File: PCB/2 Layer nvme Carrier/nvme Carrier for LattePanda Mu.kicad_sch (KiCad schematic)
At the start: 8 parts

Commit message: Parts change for BOM
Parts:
- H71, H72, H73, H74: footprint A_HDJ_Library:MountingHole_3.2mm_M3_Pad_Via -> MountingHole:MountingHole_4mm_Pad_Via
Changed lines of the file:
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@@
 			)
 		)
-		(property "Footprint" "A_HDJ_Library:MountingHole_3.2mm_M3_Pad_Via"
+		(property "Footprint" "MountingHole:MountingHole_4mm_Pad_Via"
 			(at 557.53 336.55 0)
 			(effects
@@
 		)
 		(property "Sim.Type" ""
+			(at 557.53 336.55 0)
+			(effects
+				(font
+					(size 1.27 1.27)
+				)
+				(hide yes)
+			)
+		)
+		(property "Mfr.# " ""
+			(at 557.53 336.55 0)
+			(effects
+				(font
+					(size 1.27 1.27)
+				)
+				(hide yes)
+			)
+		)
+		(property "Part#" ""
 			(at 557.53 336.55 0)
 			(effects
@@
 			)
 		)
+		(property "Mfr.# " ""
+			(at 473.71 336.55 0)
+			(effects
+				(font
+					(size 1.27 1.27)
+				)
+				(hide yes)
+			)
+		)
+		(property "Part#" ""
+			(at 473.71 336.55 0)
+			(effects
+				(font
+					(size 1.27 1.27)
+				)
+				(hide yes)
+			)
+		)
 		(pin "1"
 		)
@@
 			)
 		)
-		(property "Footprint" "A_HDJ_Library:MountingHole_3.2mm_M3_Pad_Via"
+		(property "Footprint" "MountingHole:MountingHole_4mm_Pad_Via"
 			(at 532.13 349.25 0)
 			(effects
@@
 		)
 		(property "Sim.Type" ""
+			(at 532.13 349.25 0)
+			(effects
+				(font
+					(size 1.27 1.27)
+				)
+				(hide yes)
+			)
+		)
+		(property "Mfr.# " ""
+			(at 532.13 349.25 0)
+			(effects
+				(font
+					(size 1.27 1.27)
+				)
+				(hide yes)
+			)
+		)
+		(property "Part#" ""
 			(at 532.13 349.25 0)
 			(effects
@@
 			)
 		)
+		(property "Mfr.# " ""
+			(at 499.11 349.25 0)
+			(effects
+				(font
+					(size 1.27 1.27)
+				)
+				(hide yes)
+			)
+		)
+		(property "Part#" ""
+			(at 499.11 349.25 0)
+			(effects
+				(font
+					(size 1.27 1.27)
+				)
+				(hide yes)
+			)
+		)
 		(pin "1"
 		)
@@
 			)
 		)
-		(property "Footprint" "A_HDJ_Library:MountingHole_3.2mm_M3_Pad_Via"
+		(property "Footprint" "MountingHole:MountingHole_4mm_Pad_Via"
 			(at 532.13 336.55 0)
 			(effects
@@
 		)
 		(property "Sim.Type" ""
+			(at 532.13 336.55 0)
+			(effects
+				(font
+					(size 1.27 1.27)
+				)
+				(hide yes)
+			)
+		)
+		(property "Mfr.# " ""
+			(at 532.13 336.55 0)
+			(effects
+				(font
+					(size 1.27 1.27)
+				)
+				(hide yes)
+			)
+		)
+		(property "Part#" ""
 			(at 532.13 336.55 0)
 			(effects
@@
 			)
 		)
-		(property "Footprint" "A_HDJ_Library:MountingHole_3.2mm_M3_Pad_Via"
+		(property "Footprint" "MountingHole:MountingHole_4mm_Pad_Via"
 			(at 557.53 349.25 0)
 			(effects
@@
 		)
 		(property "Sim.Type" ""
+			(at 557.53 349.25 0)
+			(effects
+				(font
+					(size 1.27 1.27)
+				)
+				(hide yes)
+			)
+		)
+		(property "Mfr.# " ""
+			(at 557.53 349.25 0)
+			(effects
+				(font
+					(size 1.27 1.27)
+				)
+				(hide yes)
+			)
+		)
+		(property "Part#" ""
 			(at 557.53 349.25 0)
 			(effects
@@
 			)
 		)
+		(property "Mfr.# " ""
+			(at 473.71 349.25 0)
+			(effects
+				(font
+					(size 1.27 1.27)
+				)
+				(hide yes)
+			)
+		)
+		(property "Part#" ""
+			(at 473.71 349.25 0)
+			(effects
+				(font
+					(size 1.27 1.27)
+				)
+				(hide yes)
+			)
+		)
 		(pin "1"
 		)
@@
 			(at 499.11 336.55 0)
 			(effects
+				(font
+					(size 1.27 1.27)
+				)
+				(hide yes)
+			)
+		)
+		(property "Mfr.# " ""
+			(at 499.11 336.55 0)
+			(effects
+				(font
+					(size 1.27 1.27)
+				)
+				(hide yes)
+			)
+		)
+		(property "Part#" ""
+			(at 499.11 336.55 0)
+			(effects

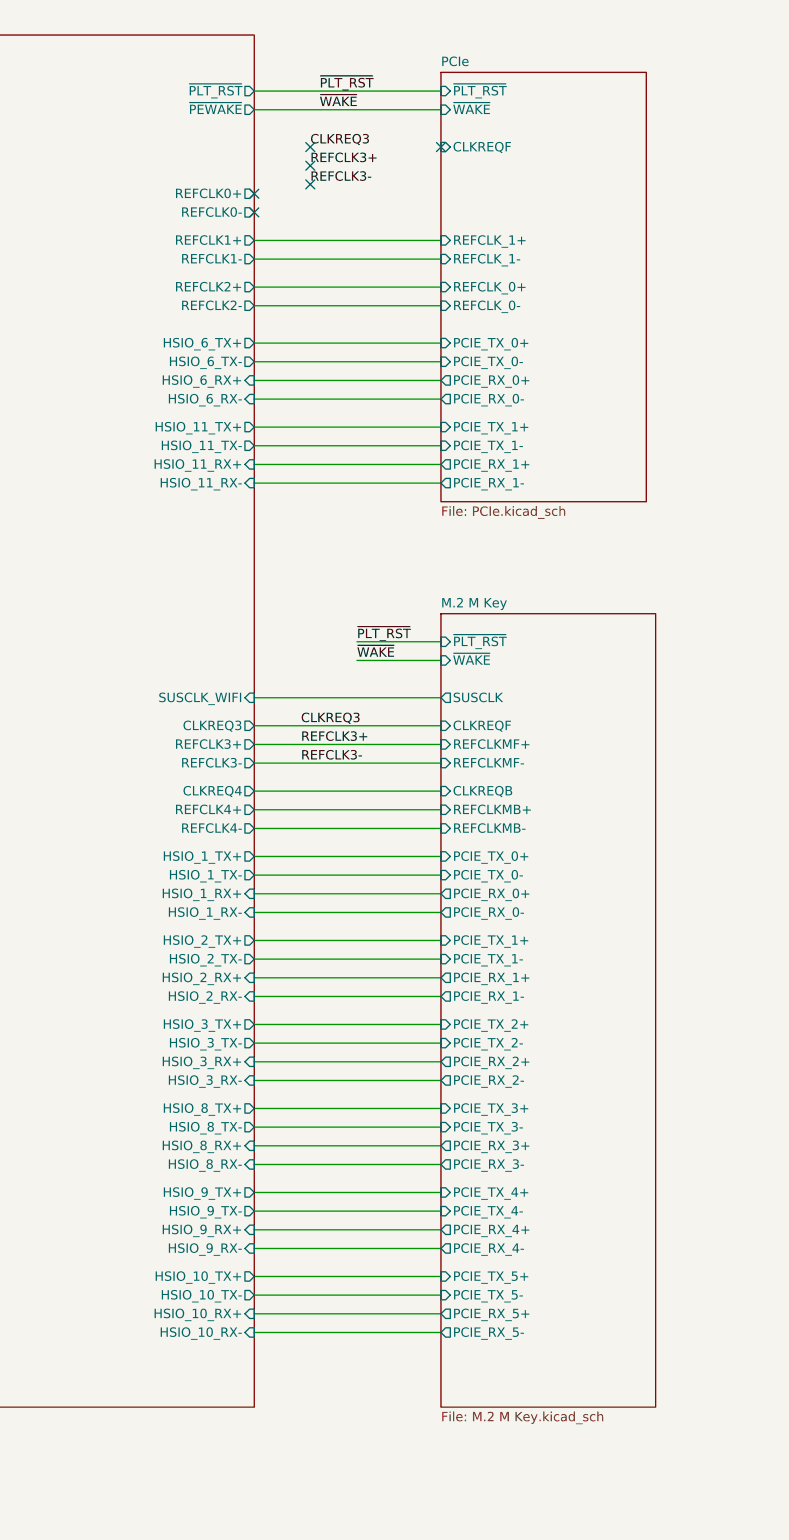
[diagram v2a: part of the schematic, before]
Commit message: Rework for PSU and REFCLK
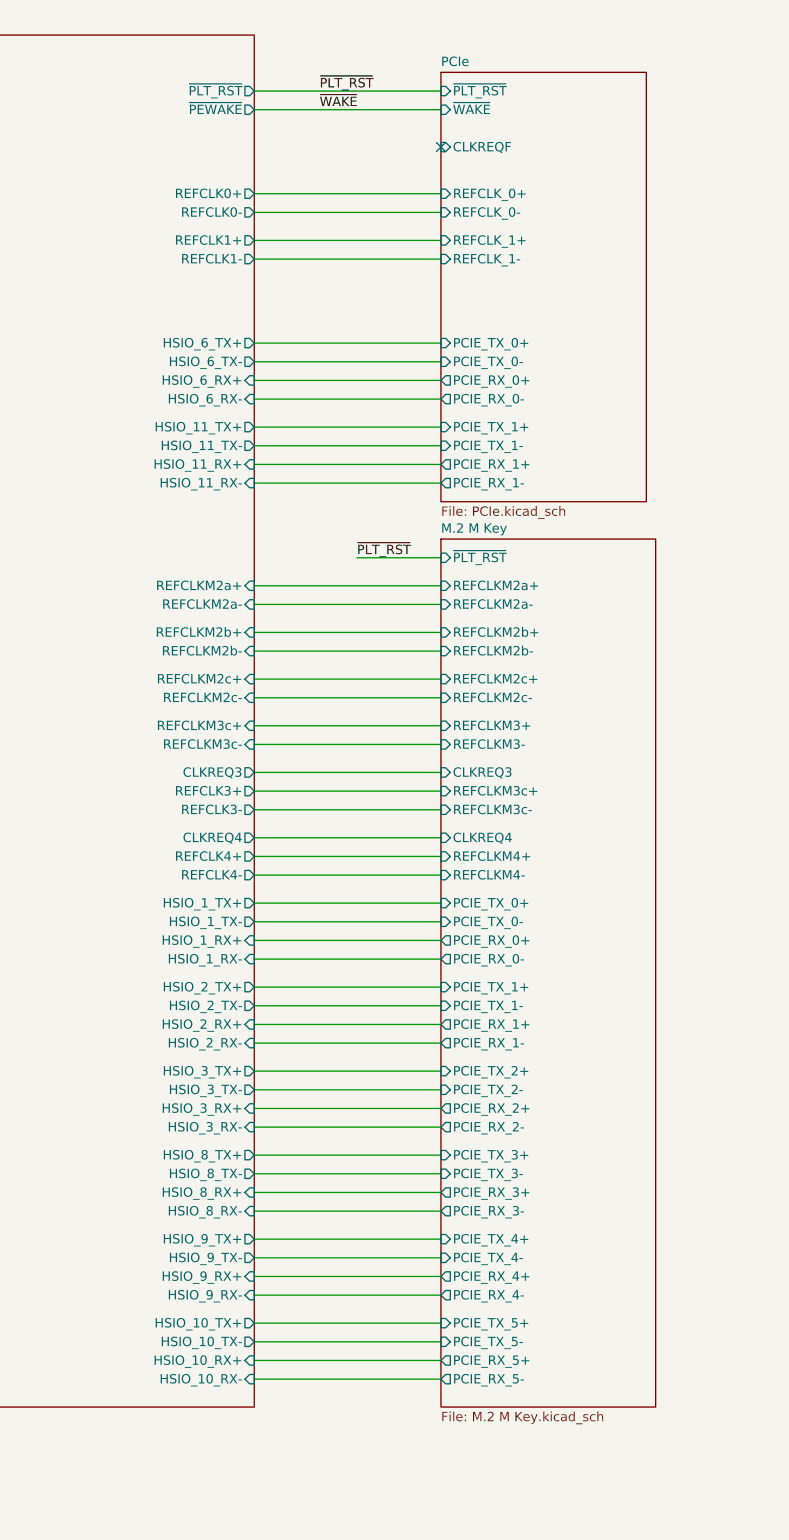
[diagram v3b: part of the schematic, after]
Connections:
- no-connect marks 7 -> 2
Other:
- sheet LattePanda Module ports: added REFCLKM2a+, REFCLKM2a-, REFCLKM2b+, REFCLKM2b-, REFCLKM2c+, REFCLKM2c-, REFCLKM3c+, REFCLKM3c-; removed REFCLK2+, REFCLK2-, SUSCLK_WIFI
- sheet M.2 M Key ports: added CLKREQ3, CLKREQ4, REFCLKM2a+, REFCLKM2a-, REFCLKM2b+, REFCLKM2b-, REFCLKM2c+, REFCLKM2c-, REFCLKM3+, REFCLKM3-, REFCLKM3c+, REFCLKM3c-, REFCLKM4+, REFCLKM4-; removed CLKREQB, CLKREQF, REFCLKMB+, REFCLKMB-, REFCLKMF+, REFCLKMF-, SUSCLK, ~{WAKE}

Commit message: Rework started with PCIe
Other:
- added sheet BIOS (BIOS.kicad_sch)
- added sheet PCIe CLK Buffer (PCIe CLK Buffer.kicad_sch)
- sheet LattePanda Module ports: added REFCLK2+, REFCLK2-, SPI-CS, SPI-IO0, SPI-IO1, SPI-IO2, SPI-IO3, SPI_CLK; removed REFCLKM2a+, REFCLKM2a-, REFCLKM2b+, REFCLKM2b-, REFCLKM2c+, REFCLKM2c-, REFCLKM3c+, REFCLKM3c-
- sheet M.2 M Key ports: added CLKREQM0, CLKREQM1, CLKREQM2, CLKREQM3, ~{WAKE}; removed none

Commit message: PCIe and CLK Buffenr Lines
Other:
- sheet M.2 M Key ports: added CLKREQM4, CLKREQM5, REFCLKM0+, REFCLKM0-, REFCLKM1+, REFCLKM1-, REFCLKM2+, REFCLKM2-, REFCLKM5+, REFCLKM5-; removed CLKREQ3, CLKREQ4, REFCLKM2a+, REFCLKM2a-, REFCLKM2b+, REFCLKM2b-, REFCLKM2c+, REFCLKM2c-, REFCLKM3c+, REFCLKM3c-
- sheet PCIe CLK Buffer ports: added CLKREQB0, CLKREQB1, CLKREQB2, CLKREQB3, REFCLKB0+, REFCLKB0-, REFCLKB1+, REFCLKB1-, REFCLKB2+, REFCLKB2-, REFCLKB3+, REFCLKB3-, REFCLK_IN+, REFCLK_IN-; removed CLKREQM0, CLKREQM1, CLKREQM2, CLKREQM3, REFCLK2+, REFCLK2-, REFCLKM0+, REFCLKM0-, REFCLKM1+, REFCLKM1-, REFCLKM2+, REFCLKM2-, REFCLKM3+, REFCLKM3-
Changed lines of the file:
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@@
 			)
 		)
-		(pin "CLKREQ3" output
+		(pin "CLKREQM0" output
 			(at 367.03 265.43 180)
 			(effects
@@
 			)
 		)
-		(pin "REFCLKM2c+" input
+		(pin "REFCLKM4+" input
 			(at 367.03 331.47 180)
 			(effects
@@
 			)
 		)
-		(pin "REFCLKM2c-" input
+		(pin "REFCLKM4-" input
 			(at 367.03 334.01 180)
 			(effects
@@
 			)
 		)
+		(pin "REFCLKM5+" input
+			(at 367.03 340.36 180)
+			(effects
+				(font
+					(size 1.27 1.27)
+				)
+				(justify left)
+			)
+		)
+		(pin "REFCLKM5-" input
+			(at 367.03 342.9 180)
+			(effects
+				(font
+					(size 1.27 1.27)
+				)
+				(justify left)
+			)
+		)
 		(pin "REFCLKM3+" input
-			(at 367.03 340.36 180)
+			(at 367.03 322.58 180)
 			(effects
 				(font
@@
 		)
 		(pin "REFCLKM3-" input
-			(at 367.03 342.9 180)
-			(effects
-				(font
-					(size 1.27 1.27)
-				)
-				(justify left)
-			)
-		)
-		(pin "REFCLKM2b+" input
-			(at 367.03 322.58 180)
-			(effects
-				(font
-					(size 1.27 1.27)
-				)
-				(justify left)
-			)
-		)
-		(pin "REFCLKM2b-" input
 			(at 367.03 325.12 180)
 			(effects
@@
 			)
 		)
-		(pin "REFCLKM4+" input
+		(pin "REFCLKM1+" input
 			(at 367.03 287.02 180)
 			(effects
@@
 			)
 		)
-		(pin "REFCLKM4-" input
+		(pin "REFCLKM1-" input
 			(at 367.03 289.56 180)
 			(effects
@@
 			)
 		)
-		(pin "CLKREQ4" output
+		(pin "CLKREQM1" output
 			(at 367.03 284.48 180)
 			(effects
@@
 			)
 		)
-		(pin "REFCLKM2a+" input
+		(pin "REFCLKM2+" input
 			(at 367.03 313.69 180)
 			(effects
@@
 			)
 		)
-		(pin "REFCLKM2a-" input
+		(pin "REFCLKM2-" input
 			(at 367.03 316.23 180)
 			(effects
@@
 			)
 		)
-		(pin "REFCLKM3c+" input
+		(pin "REFCLKM0+" input
 			(at 367.03 267.97 180)
 			(effects
@@
 			)
 		)
-		(pin "REFCLKM3c-" input
+		(pin "REFCLKM0-" input
 			(at 367.03 270.51 180)
 			(effects
@@
 			)
 		)
+		(pin "CLKREQM5" output
+			(at 367.03 337.82 180)
+			(effects
+				(font
+					(size 1.27 1.27)
+				)
+				(justify left)
+			)
+		)
+		(pin "CLKREQM2" output
+			(at 367.03 311.15 180)
+			(effects
+				(font
+					(size 1.27 1.27)
+				)
+				(justify left)
+			)
+		)
+		(pin "CLKREQM4" output
+			(at 367.03 328.93 180)
+			(effects
+				(font
+					(size 1.27 1.27)
+				)
+				(justify left)
+			)
+		)
 		(pin "CLKREQM3" output
-			(at 367.03 337.82 180)
-			(effects
-				(font
-					(size 1.27 1.27)
-				)
-				(justify left)
-			)
-		)
-		(pin "CLKREQM0" output
-			(at 367.03 311.15 180)
-			(effects
-				(font
-					(size 1.27 1.27)
-				)
-				(justify left)
-			)
-		)
-		(pin "CLKREQM2" output
-			(at 367.03 328.93 180)
-			(effects
-				(font
-					(size 1.27 1.27)
-				)
-				(justify left)
-			)
-		)
-		(pin "CLKREQM1" output
 			(at 367.03 320.04 180)
 			(effects
@@
 			)
 		)
-		(pin "CLKREQM0" input
+		(pin "REFCLKB0+" output
+			(at 195.58 313.69 0)
+			(effects
+				(font
+					(size 1.27 1.27)
+				)
+				(justify right)
+			)
+		)
+		(pin "REFCLKB0-" output
+			(at 195.58 316.23 0)
+			(effects
+				(font
+					(size 1.27 1.27)
+				)
+				(justify right)
+			)
+		)
+		(pin "REFCLKB2+" output
+			(at 195.58 331.47 0)
+			(effects
+				(font
+					(size 1.27 1.27)
+				)
+				(justify right)
+			)
+		)
+		(pin "REFCLKB1+" output
+			(at 195.58 322.58 0)
+			(effects
+				(font
+					(size 1.27 1.27)
+				)
+				(justify right)
+			)
+		)
+		(pin "REFCLKB1-" output
+			(at 195.58 325.12 0)
+			(effects
+				(font
+					(size 1.27 1.27)
+				)
+				(justify right)
+			)
+		)
+		(pin "REFCLKB2-" output
+			(at 195.58 334.01 0)
+			(effects
+				(font
+					(size 1.27 1.27)
+				)
+				(justify right)
+			)
+		)
+		(pin "REFCLK_IN-" input
+			(at 195.58 295.91 0)
+			(effects
+				(font
+					(size 1.27 1.27)
+				)
+				(justify right)
+			)
+		)
+		(pin "REFCLK_IN+" input
+			(at 195.58 293.37 0)
+			(effects
+				(font
+					(size 1.27 1.27)
+				)
+				(justify right)
+			)
+		)
+		(pin "CLKREQB0" input
 			(at 195.58 311.15 0)
 			(effects
@@
 			)
 		)
-		(pin "CLKREQM3" input
+		(pin "REFCLKB3-" output
+			(at 195.58 342.9 0)
+			(effects
+				(font
+					(size 1.27 1.27)
+				)
+				(justify right)
+			)
+		)
+		(pin "REFCLKB3+" output
+			(at 195.58 340.36 0)
+			(effects
+				(font
+					(size 1.27 1.27)
+				)
+				(justify right)
+			)
+		)
+		(pin "CLKREQB3" input
 			(at 195.58 337.82 0)
 			(effects
@@
 			)
 		)
-		(pin "REFCLKM3-" output
-			(at 195.58 342.9 0)
-			(effects
-				(font
-					(size 1.27 1.27)
-				)
-				(justify right)
-			)
-		)
-		(pin "REFCLKM3+" output
-			(at 195.58 340.36 0)
-			(effects
-				(font
-					(size 1.27 1.27)
-				)
-				(justify right)
-			)
-		)
-		(pin "REFCLK2+" input
-			(at 195.58 293.37 0)
-			(effects
-				(font
-					(size 1.27 1.27)
-				)
-				(justify right)
-			)
-		)
-		(pin "REFCLK2-" input
-			(at 195.58 295.91 0)
-			(effects
-				(font
-					(size 1.27 1.27)
-				)
-				(justify right)
-			)
-		)
-		(pin "REFCLKM1+" output
-			(at 195.58 322.58 0)
-			(effects
-				(font
-					(size 1.27 1.27)
-				)
-				(justify right)
-			)
-		)
-		(pin "REFCLKM1-" output
-			(at 195.58 325.12 0)
-			(effects
-				(font
-					(size 1.27 1.27)
-				)
-				(justify right)
-			)
-		)
-		(pin "REFCLKM2+" output
-			(at 195.58 331.47 0)
-			(effects
-				(font
-					(size 1.27 1.27)
-				)
-				(justify right)
-			)
-		)
-		(pin "REFCLKM2-" output
-			(at 195.58 334.01 0)
-			(effects
-				(font
-					(size 1.27 1.27)
-				)
-				(justify right)
-			)
-		)
-		(pin "REFCLKM0+" output
-			(at 195.58 313.69 0)
-			(effects
-				(font
-					(size 1.27 1.27)
-				)
-				(justify right)
-			)
-		)
-		(pin "REFCLKM0-" output
-			(at 195.58 316.23 0)
-			(effects
-				(font
-					(size 1.27 1.27)
-				)
-				(justify right)
-			)
-		)
-		(pin "CLKREQM2" input
+		(pin "CLKREQB1" input
+			(at 195.58 320.04 0)
+			(effects
+				(font
+					(size 1.27 1.27)
+				)
+				(justify right)
+			)
+		)
+		(pin "CLKREQB2" input
 			(at 195.58 328.93 0)
 			(effects
 				(font
-					(size 1.27 1.27)
-				)
-				(justify right)
-			)
-		)
-		(pin "CLKREQM1" input
-			(at 195.58 320.04 0)
-			(effects
-				(font
